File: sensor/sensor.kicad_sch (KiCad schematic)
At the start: 44 parts, among them IC1 MAX30002CWV+, IC2 LP5900TLX-2.7_NOPB, IC3 MAX86141ENP+T, IC4 SIT1532AC, IC5 LP5900TLX-1.8_NOPB, J1 Conn_01x10_Female, J2 Conn_01x10_Female, J3 Probe_01_male, J4 Probe_01_male, J5 Probe_01_male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

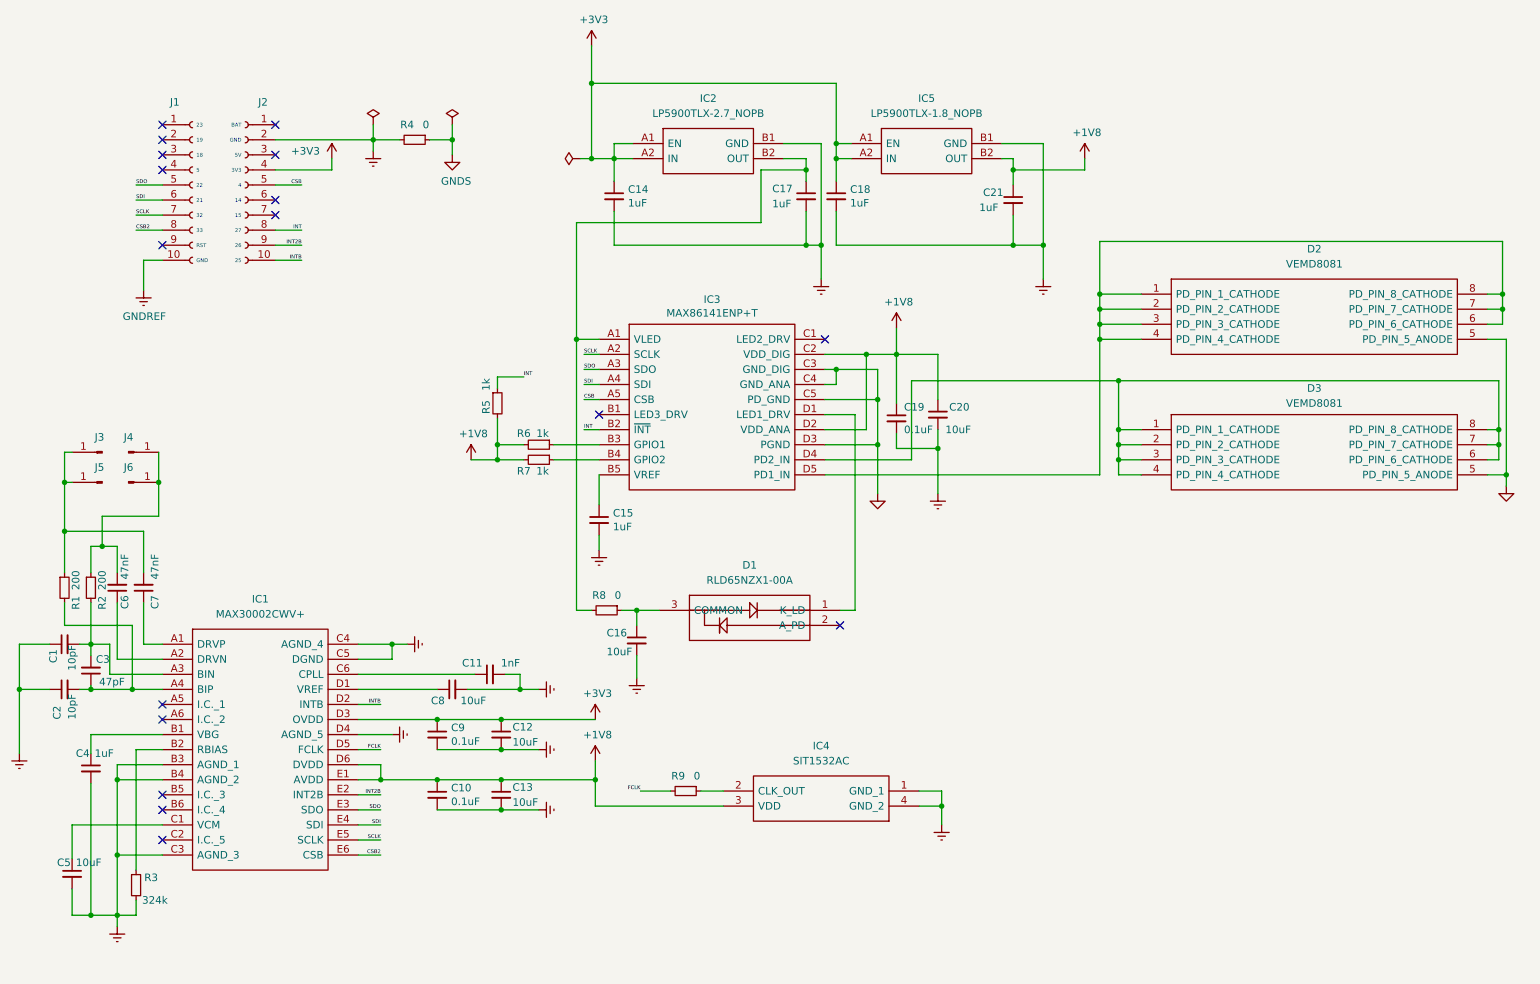
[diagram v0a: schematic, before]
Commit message: Clean up for old files. Reposition schematic components to 50mil grid. No errors and warnings for SCH. PCB is next.
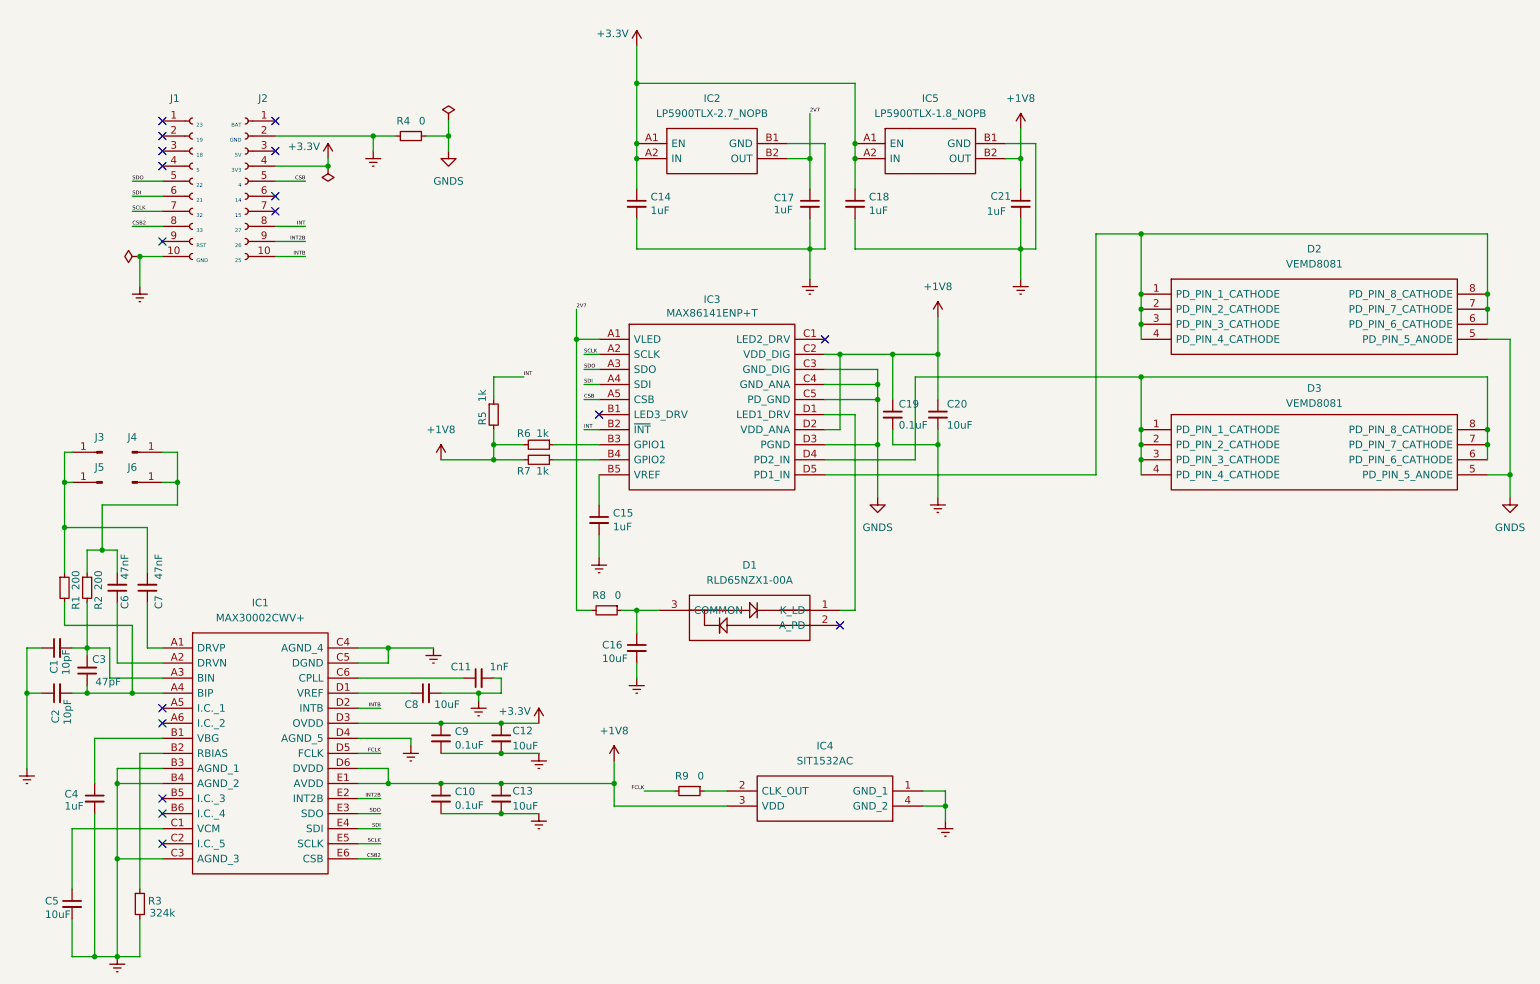
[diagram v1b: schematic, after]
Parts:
- IC3: symbol sensor-rescue:MAX86141ENP+-Horace -> Horace:MAX86141ENP+; Manufacturer_Name (none) -> Maxim Integrated; Manufacturer_Part_Number (none) -> MAX86141ENP+; Mouser Part Number 700-MAX86141ENP+T -> 700-MAX86141ENP+; Mouser Price/Stock https://www.mouser.ee/ProductDetail/Maxim-Integrated/MAX861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 -> https://www.mouser.co.uk/ProductDetail/Maxim-Integrated/MAX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
- J1, J2: symbol Connector:Conn_01x10_Female -> Connector:Conn_01x10_Socket
- J3, J4, J5, J6: symbol sensor-rescue:Probe_01_male-Horace -> Horace:Probe_01_male
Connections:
- net 2V7: now reaches C17.1, IC2.B2 (OUT), IC3.A1 (VLED), R8.2
- net +3V3 renamed +3.3V
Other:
- moved on the sheet: C1, C10, C11, C12, C13, C14, C16, C17, C18, C19, C2, C21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

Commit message: label external clock
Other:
- note added: "32768Hz"
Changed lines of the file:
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@@
 	(text "25"
 		(exclude_from_sim no)
-		(at 57.785 62.23 180)
+		(at 57.785 62.23 0)
 		(effects
 			(font
@@
 	(text "BAT"
 		(exclude_from_sim no)
-		(at 57.785 39.37 180)
+		(at 57.785 39.37 0)
 		(effects
 			(font
@@
 	(text "GND"
 		(exclude_from_sim no)
-		(at 57.785 41.91 180)
+		(at 57.785 41.91 0)
 		(effects
 			(font
@@
 	(text "26"
 		(exclude_from_sim no)
-		(at 57.785 59.69 180)
+		(at 57.785 59.69 0)
 		(effects
 			(font
@@
 	(text "4"
 		(exclude_from_sim no)
-		(at 57.785 49.53 180)
+		(at 57.785 49.53 0)
 		(effects
 			(font
@@
 		)
 	)
+	(text "32768Hz"
+		(exclude_from_sim no)
+		(at 156.21 157.734 0)
+		(effects
+			(font
+				(size 0.762 0.762)
+			)
+		)
+	)
 	(text "27"
 		(exclude_from_sim no)
-		(at 57.785 57.15 180)
+		(at 57.785 57.15 0)
 		(effects
 			(font
@@
 	(text "3V3"
 		(exclude_from_sim no)
-		(at 57.785 46.99 180)
+		(at 57.785 46.99 0)
 		(effects
 			(font
@@
 	(text "5V"
 		(exclude_from_sim no)
-		(at 57.785 44.45 180)
+		(at 57.785 44.45 0)
 		(effects
 			(font
@@
 	(text "15"
 		(exclude_from_sim no)
-		(at 57.785 54.61 180)
+		(at 57.785 54.61 0)
 		(effects
 			(font
@@
 	(text "14"
 		(exclude_from_sim no)
-		(at 57.785 52.07 180)
+		(at 57.785 52.07 0)
 		(effects
 			(font
